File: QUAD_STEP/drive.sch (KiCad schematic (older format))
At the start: 17 parts

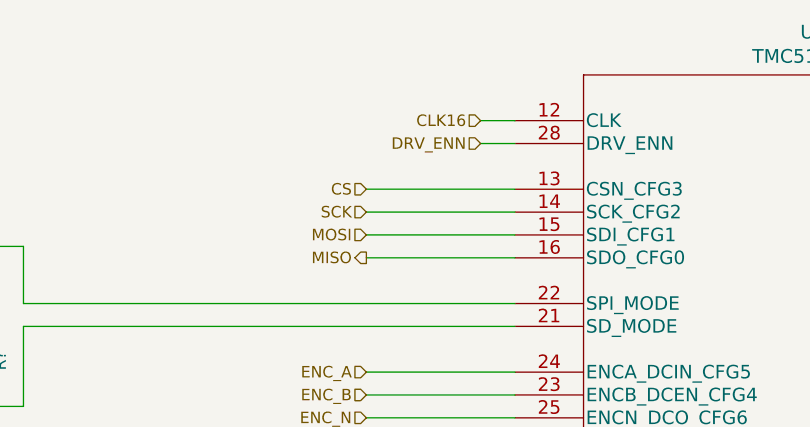
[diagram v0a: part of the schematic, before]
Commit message: added more components, fleshed out DB-25 interface, added PSoC
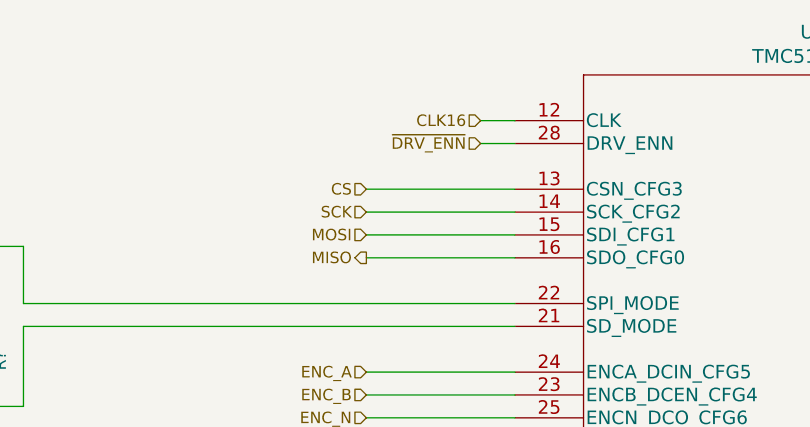
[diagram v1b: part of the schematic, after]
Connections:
- net DRV_ENN renamed ~DRV_ENN
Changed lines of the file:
@@
 $Descr A4 11693 8268
 encoding utf-8
-Sheet 5 7
+Sheet 2 13
 Title ""
 Date ""
@@
 CLK16
 Text HLabel 3950 1450 0    50   Input ~ 0
-DRV_ENN
+~DRV_ENN
 Text HLabel 3450 1950 0    50   Output ~ 0
 MISO
